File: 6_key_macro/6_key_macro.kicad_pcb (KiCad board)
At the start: 2 copper layers, 85 x 55 mm, 37 parts, among them J1 SWD, P1 USB_C_Plug_USB2.0, Q1 DMG1012T, SW1 CherryMX_LED, SW2 CherryMX_LED, SW3 CherryMX_LED, SW4 CherryMX_LED, SW5 CherryMX_LED, SW6 CherryMX_LED, U1 STM32F042K6Tx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

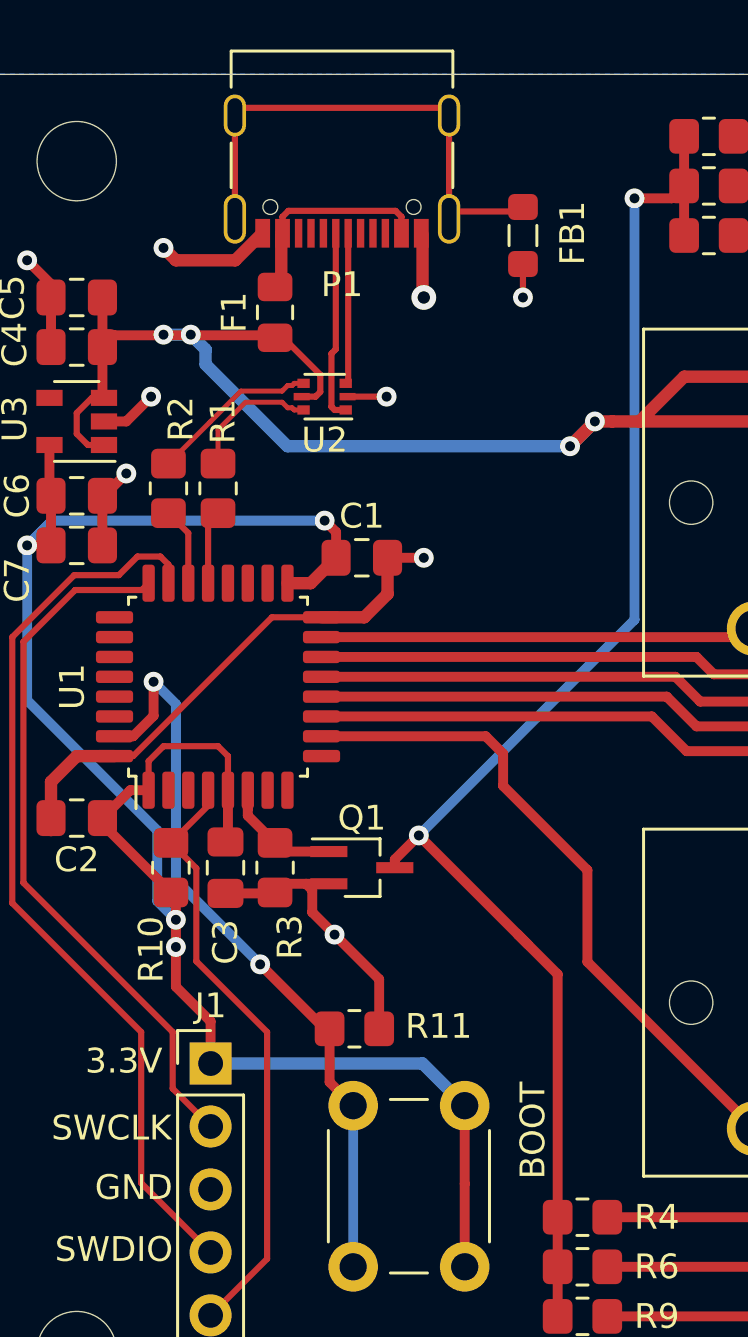
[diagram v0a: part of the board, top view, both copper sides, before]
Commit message: added 5.1k resistors to cc1 and cc2 for usb-c to usb-c compatibility
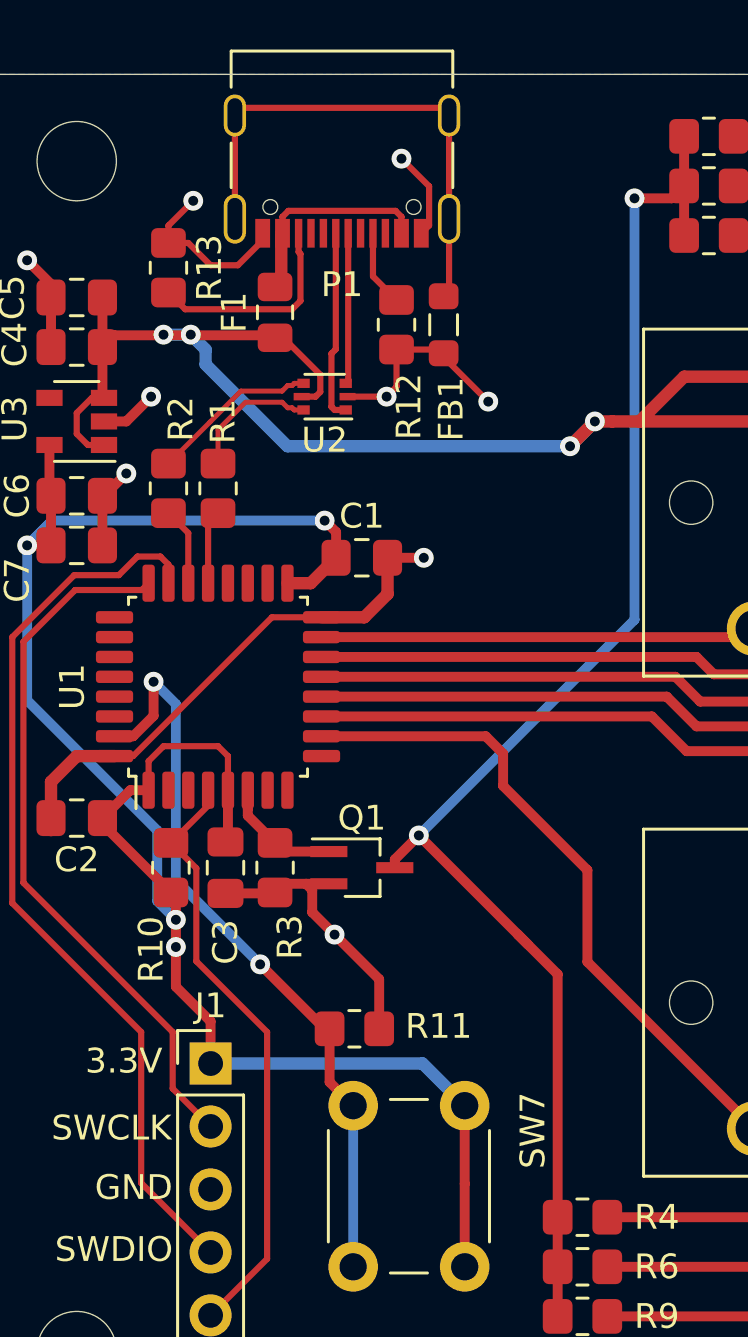
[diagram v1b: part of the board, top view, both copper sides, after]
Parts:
- added R12: 5.1k, Resistor_SMD:R_0805_2012Metric_Pad1.20x1.40mm_HandSolder, F.Cu at (72.4, 125.1)
- added R13: 5.1k, Resistor_SMD:R_0805_2012Metric_Pad1.20x1.40mm_HandSolder, F.Cu at (63.2, 122.8)
- moved FB1 4.82 mm to (74.3, 125.1)
- renumbered BOOT to SW7
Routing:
- net GND: track 53.0 -> 61.8 mm
- net Net-(P1-PadB5): track 0.00 -> 8.50 mm
- net Net-(P1-PadA5): track 0.00 -> 3.08 mm

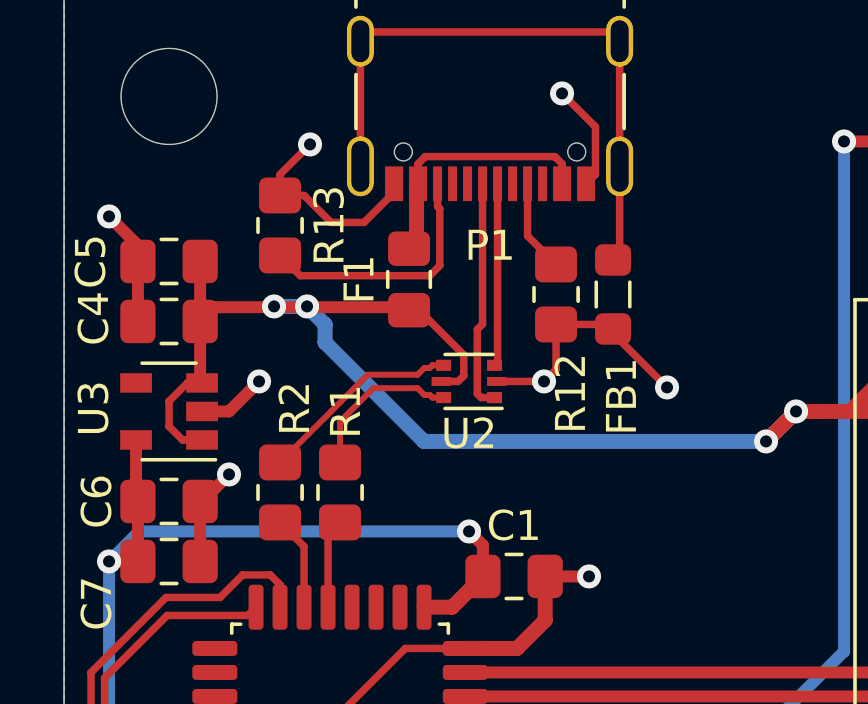
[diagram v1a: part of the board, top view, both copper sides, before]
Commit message: swapped tvs diodes
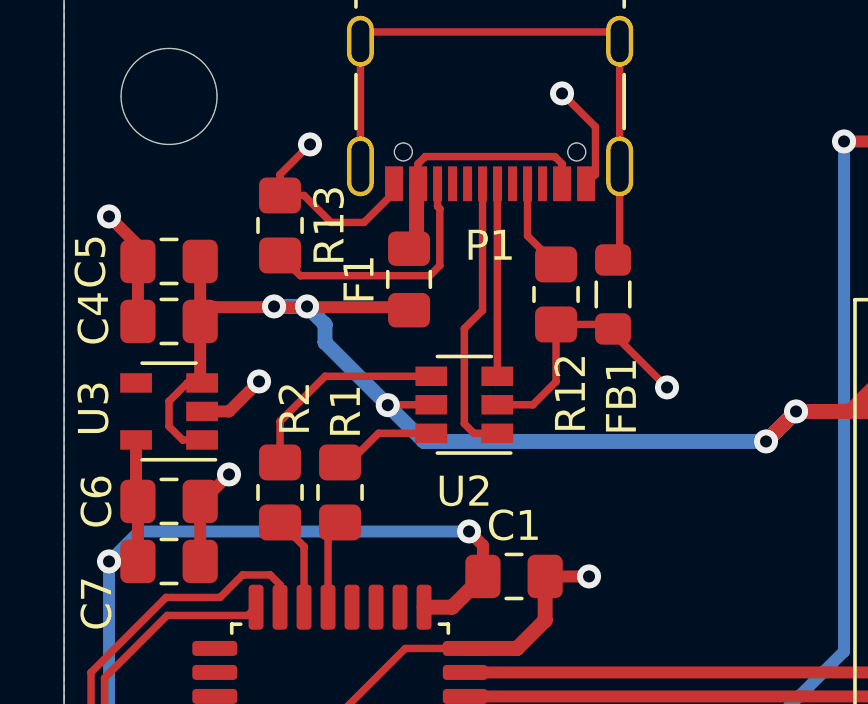
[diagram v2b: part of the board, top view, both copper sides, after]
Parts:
- U2: value USBLC6-2P6 -> USBLC6-2SC6; footprint Package_TO_SOT_SMD:SOT-666 -> Package_TO_SOT_SMD:SOT-23-6
- moved U2 0.79 mm to (69.3, 128.8)
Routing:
- net VBUS: track 173.8 -> 171.3 mm, vias 4 -> 5
- net /USB_D-: track 5.40 -> 3.44 mm
- net Net-(P1-PadA7): track 7.67 -> 9.48 mm
- net GND: track 61.8 -> 62.4 mm, vias 9 -> 8
